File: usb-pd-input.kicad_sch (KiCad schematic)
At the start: 15 parts, among them J1 USB-C, Q1 -30V -4A, U1 STUSB4500QTR

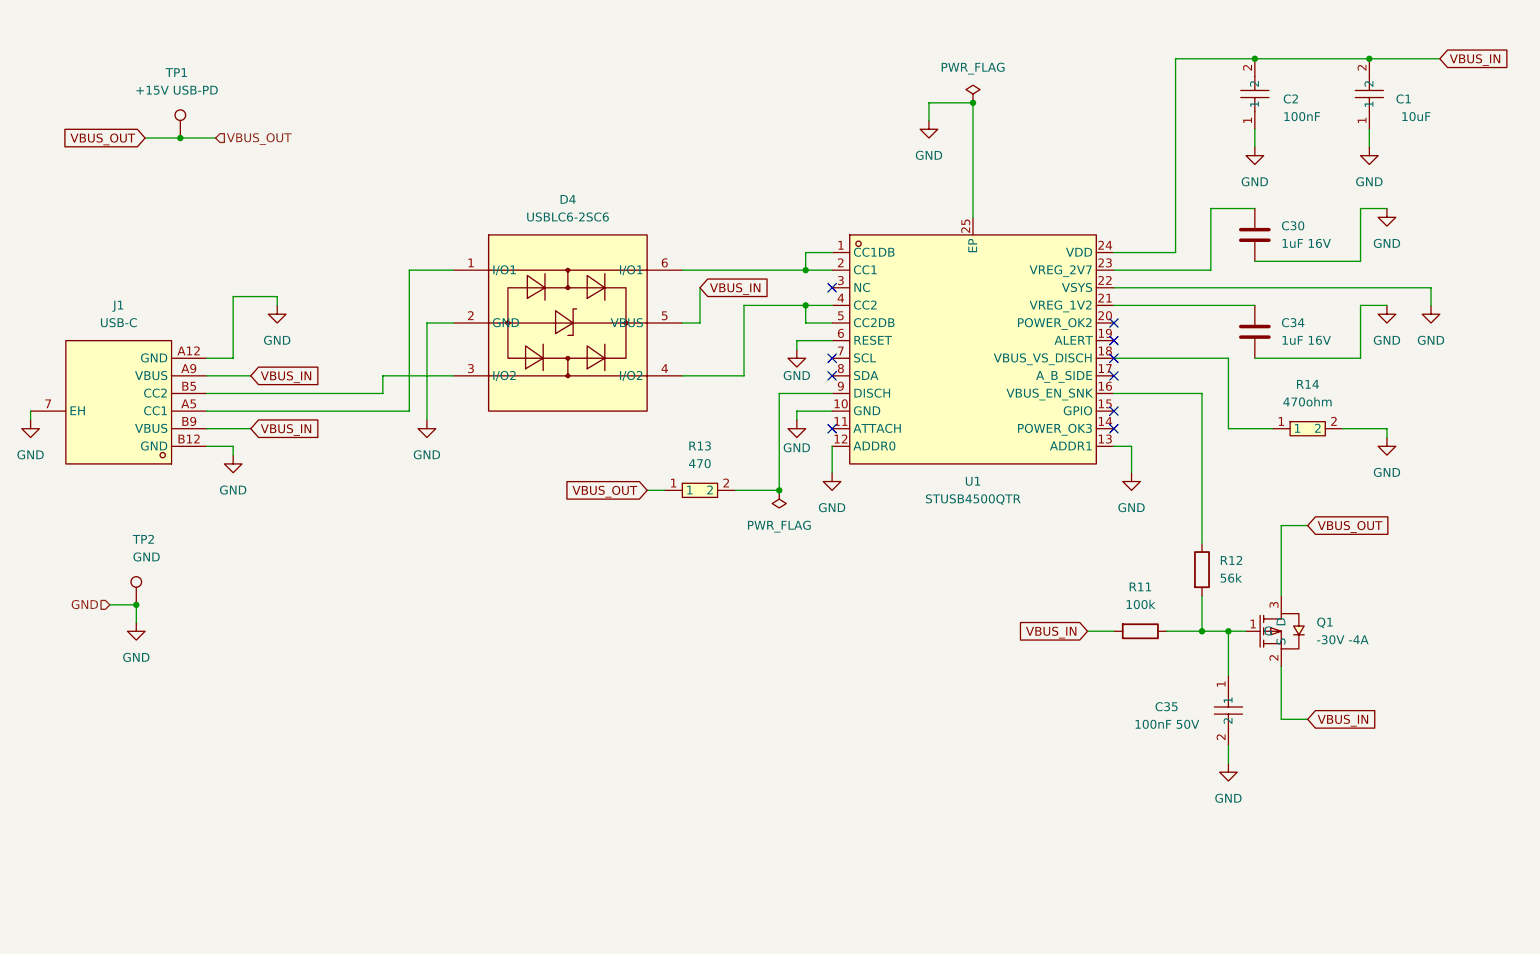
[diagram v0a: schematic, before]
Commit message: feat: Add I2C programming pads (J2, R15, R16) for STUSB4500 NVM programming
Add J2 pogo pad connector (1x4, 2.54mm) with SCL, SDA, GND, NC pins
at board edge for STUSB4500 NVM programming via pogo pin clip. Add R15
and R16 (4.7k) I2C pull-up resistors to VREG_2V7. Connect previously
NC pins SCL (pin 7) and SDA (pin 8) to J2 pads.
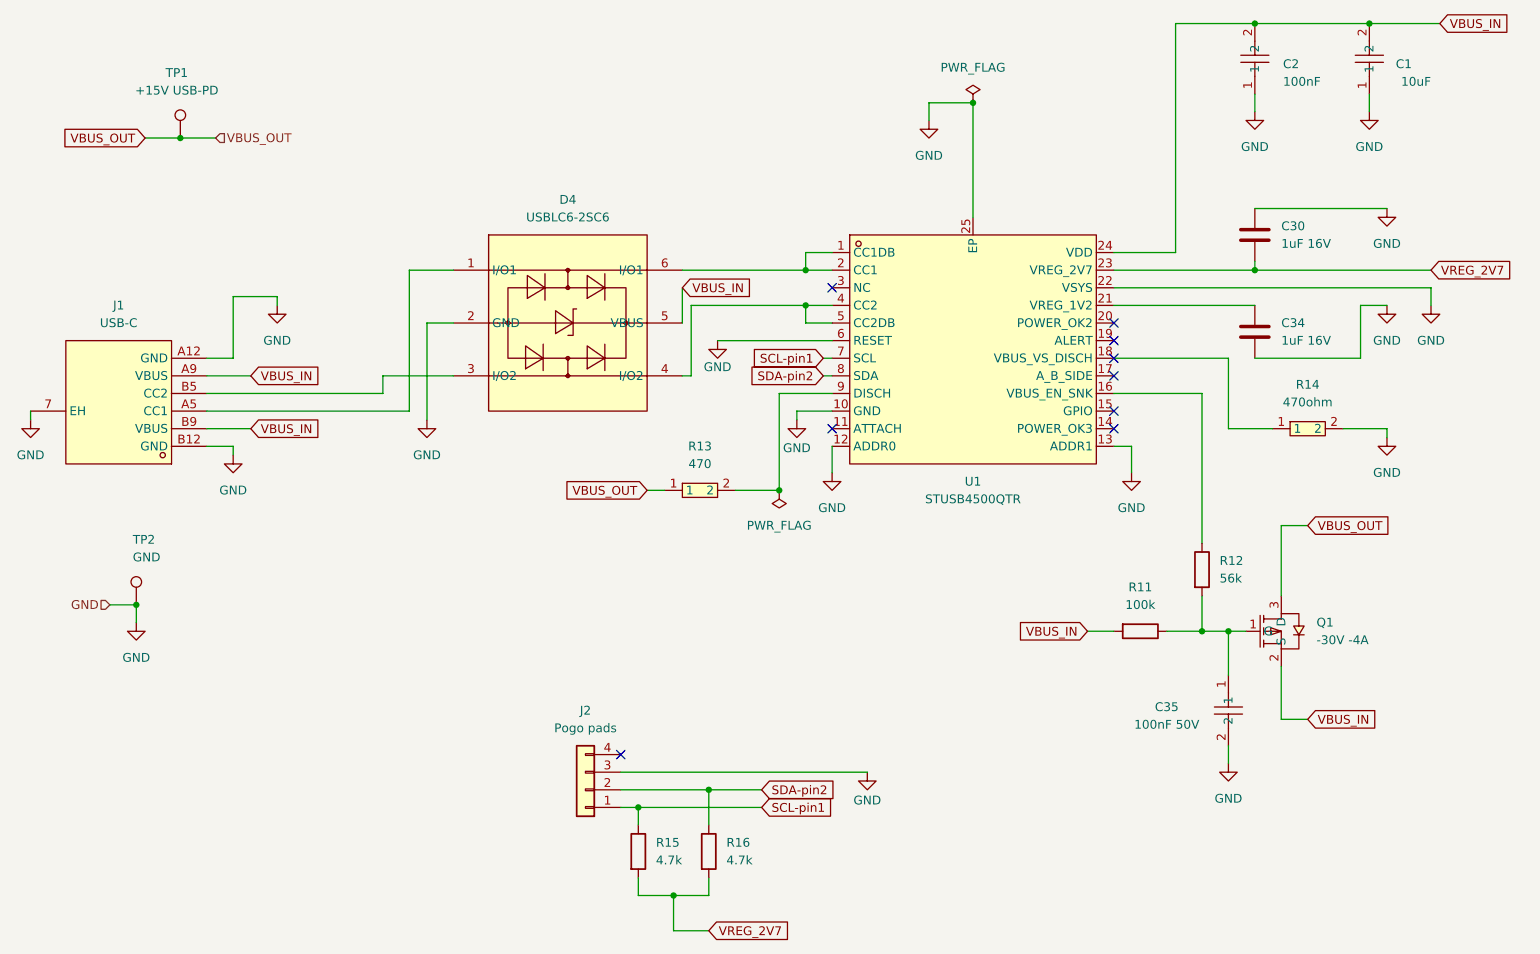
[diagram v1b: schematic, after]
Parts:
- added J2: Pogo pads, symbol Connector_Generic:Conn_01x04
- added R15, R16: 4.7k, symbol Device:R
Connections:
- net GND: now also C30.1, J2.3 (Pin_3); no longer C30.2
- net VREG_2V7: now reaches U1.23 (VREG_2V7)
- net VREG_2V7: now also C30.2, R15.2, R16.2; no longer C30.1
- net SCL-pin1: now reaches U1.7 (SCL)
- net SCL-pin1: now also J2.1 (Pin_1), R15.1
- net SDA-pin2: now reaches U1.8 (SDA)
- net SDA-pin2: now also J2.2 (Pin_2), R16.1
- no-connect marks 10 -> 9
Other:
- moved on the sheet: C1, C2
